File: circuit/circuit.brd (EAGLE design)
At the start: 100 x 80 mm, 56 parts, among them IC1 74HC86N, IC2 74HC86N, IC3 74HC30N, IC4 74HC86N

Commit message: updated circuit (layout needs to be done next)
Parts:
- removed CM4, CM5, CM6: 100nF, rcl:C025-025X050
- removed H1, H2, H3, H4: MOUNT-HOLE3.2, holes:3,2
- removed IC2, IC4: 74HC86N, 74xx-eu:DIL14
- removed IC3: 74HC30N, 74xx-eu:DIL14
- removed JP1: IN, pinhead:1X08
- removed JT: (no value), pinhead:1X04
- removed SJ1, SJ2, SJ3, SJ4, SJ5, SJ6, SJ7, SJ8: (no value), jumper:SJ
- added CS4: 100nF, rcl:C025-025X050
- added LD1, LD2: green, robo_ag:LED_3MM
- added LD3, LD4: yellow, robo_ag:LED_3MM
- added RLD1, RLD2, RLD3, RLD4: 2k, rcl:0207/10
- added RN1, RN2, RN3, RN4: 120, resistor-sil:SIL8
- added RP1: 300, rcl:0207/10
- added X1: PSS 254/8G, con-molex:22-23-2081
- IC1: value 74HC86N -> 74HC04N
- moved SV1 232.4 mm to (-22.2, -292.1)
- moved SV2 228.0 mm to (-22.2, -304.2)
- moved IC1 220.7 mm to (-21.6, -315.0)
- renumbered RP to RP2
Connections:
- removed net BUS_ERROR: IC3.8
- removed net DISP_COL_SCK: JP1.6
- removed net DISP_COL_SER: JP1.4
- removed net PROG_MOSI: ICM.17, RP2.2
- removed net PROG_SCK: ICM.19, JP.3
- removed net RETURN_LED_LAOD: IC2.5
- removed net TWI_SCL: ICM.28, JT.1, JT.4
- removed net TWI_SDA: ICM.27, JT.2, JT.3
- removed net VCC: IC3.14
- new net !BUS_RGB: IC1.1, IC1.3, ICM.3
- new net !RETURN_RGB: IC1.8, ICM.2
- new net N$32: IC1.10, RLD2.2
- new net N$33: JP.3, RP1.2
- new net N$34: LD2.K, RLD2.1
- new net N$35: ICM.27
- new net N$36: ICM.28
- new net N$37: IC1.6, RLD3.2
- new net N$38: LD3.K, RLD3.1
- new net N$41: IC1.12, RLD4.1
- new net N$42: LD4.A, RLD4.2
- new net PROG_MOSI_AND_DISP_COL_SER: ICM.17, RN3.3, RP2.2
- new net PROG_SCK_AND_DISP_COL_SCK: ICM.19, RN3.7, RP1.1
- net +5V: now also CS4.1, LD2.A, LD3.A, X1.2; no longer CM4.2, CM5.2, CM6.2, IC2.14, IC4.14, JP1.2, SJ8.1
- net BTN2: now also ICM.15; no longer ICM.26
- net BTN3: now also ICM.16; no longer ICM.6
- net BUS_BTN_DATA: now also ICM.4, RN1.3; no longer IC2.1, SV1.8
- net BUS_BTN_LOAD: now also ICM.5, RN2.6; no longer IC1.12, SV1.7
- net BUS_CLK: now also ICM.12, RN2.1; no longer IC1.1, SV1.2
- net BUS_IR_CLK: now also ICM.11, RN1.5; no longer IC1.9, SV1.6
- net BUS_LED_DATA: now also IC1.5, ICM.6, RN1.1; no longer IC2.9, SV1.10
- net BUS_LED_LOAD: now also ICM.13, RN2.4; no longer IC2.4, SV1.9
- net BUS_RGB: now also IC1.2, RN1.7; no longer IC1.4, SV1.4
- net DISP_!ENABLE!: now also ICM.26, RN4.3; no longer JP1.8
- net DISP_RCK: now also ICM.25, RN4.1; no longer JP1.7
- net DISP_ROW_SCK: now also ICM.24, RN3.5; no longer JP1.5
- net DISP_ROW_SER: now also ICM.23, RN3.1; no longer JP1.3
- net GND: now also CS4.2, LD1.K, LD4.K, SV1.10, SV1.6, SV1.8, SV2.10, SV2.6, SV2.8, X1.1; no longer CM4.1, CM5.1, CM6.1, IC2.12, IC2.13, IC2.7, IC3.7, IC4.7, JP1.1, SV1.1, SV1.3, SV1.5, SV2.1, SV2.3, SV2.5
- net N$1: now also RN1.2, SV1.1; no longer IC3.1, SJ1.2
- net N$16: now also RN1.8, SV1.7; no longer IC3.4, SJ4.2
- net N$17: now also RN2.2, SV1.9; no longer IC3.5, SJ5.2
- net N$18: now also RN2.5, SV1.4; no longer IC3.6, SJ6.2
- net N$19: now also RN2.3, SV1.2; no longer IC3.11, SJ7.2
- net N$2: now also RN1.4, SV1.3; no longer IC3.2, SJ2.2
- net N$20: now also RN3.2, X1.3; no longer IC3.12, SJ8.2
- net N$21: now also RN3.4, X1.4; no longer IC1.3, SJ1.1
- net N$22: now also RN3.6, X1.5; no longer IC1.6, SJ2.1
- net N$23: now also RN3.8, X1.6; no longer IC1.8, SJ3.1
- net N$24: now also RN4.2, X1.7; no longer IC1.11, SJ4.1
- net N$25: now also RN4.4, X1.8; no longer IC2.3, SJ5.1
- net N$26: now also LD1.A, RLD1.2; no longer IC2.6, SJ6.1
- net N$3: now also RN1.6, SV1.5; no longer IC3.3, SJ3.2
- net N$31: now also IC1.4, RLD1.1; no longer IC2.8, SJ7.1
- net RETURN_BTN_DATA: now also IC1.13, SV2.3; no longer IC2.2, SV2.8
- net RETURN_BTN_LOAD: now also SV2.4; no longer IC1.13, SV2.7
- net RETURN_CLK: now also SV2.9; no longer IC1.2, SV2.2
- net RETURN_IR_CLK: now also SV2.5; no longer IC1.10, SV2.6
- net RETURN_LED_DATA: now also SV2.1; no longer IC2.10, SV2.10
- net RETURN_LED_LOAD: now also SV2.2; no longer SV2.9
- net RETURN_RGB: now also IC1.11, IC1.9, SV2.7; no longer IC1.5, SV2.4
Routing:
- net PROG_SCK: track 53.1 -> 0.00 mm
- net PROG_SCK_AND_DISP_COL_SCK: track 0.00 -> 51.8 mm
- net PROG_MOSI_AND_DISP_COL_SER: track 0.00 -> 41.1 mm
- net PROG_MOSI: track 41.1 -> 0.00 mm
- net BTN2: track 68.5 -> 37.7 mm
- net TWI_SCL: track 15.1 -> 0.00 mm
- net TWI_SDA: track 11.8 -> 0.00 mm

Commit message: Updated Layout
Layout work in progress
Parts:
- removed RN1, RN2, RN3, RN4: 120, resistor-sil:SIL8
- added R1, R10, R11, R12, R13, R2, R3, R4, R5, R6, R7, R8, R9: 120, rcl:R0805
- moved LD4 444.7 mm to (5.71, 45.7), turned to 180 degrees
- moved RLD4 440.8 mm to (15.9, 45.1), turned to 180 degrees
- moved LD3 425.7 mm to (5.08, 36.2)
- moved RLD3 422.0 mm to (16.5, 35.6)
- moved LD1 416.9 mm to (5.71, 41.3), turned to 180 degrees
- moved LD2 411.2 mm to (5.71, 31.1)
- moved RLD1 408.7 mm to (16.5, 40.6), turned to 180 degrees
- moved RLD2 404.3 mm to (16.5, 31.8)
- moved CS4 379.4 mm to (33.7, 49.5), turned to 180 degrees
- moved IC1 358.0 mm to (33.7, 38.7), turned to 270 degrees
- moved SV2 318.6 mm to (43.2, 7.62), turned to 180 degrees
- moved SV1 302.9 mm to (21.6, 7.62), turned to 180 degrees
- moved RP1 301.5 mm to (81.6, 33.7)
- moved X1 278.4 mm to (73.0, 7.30)
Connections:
- removed net N$35: ICM.27
- removed net N$36: ICM.28
- net BTN1: now also ICM.27; no longer ICM.14
- net BTN2: now also ICM.28; no longer ICM.15
- net BUS_BTN_DATA: now also R8.1; no longer RN1.3
- net BUS_BTN_LOAD: now also R13.2; no longer RN2.6
- net BUS_CLK: now also R11.1; no longer RN2.1
- net BUS_IR_CLK: now also R9.1; no longer RN1.5
- net BUS_LED_DATA: now also R7.1; no longer RN1.1
- net BUS_LED_LOAD: now also R12.2; no longer RN2.4
- net BUS_RGB: now also R10.1; no longer RN1.7
- net DISP_!ENABLE!: now also R6.1; no longer RN4.3
- net DISP_RCK: now also R5.1; no longer RN4.1
- net DISP_ROW_SCK: now also R3.1; no longer RN3.5
- net DISP_ROW_SER: now also R1.1; no longer RN3.1
- net N$1: now also R7.2; no longer RN1.2
- net N$16: now also R10.2; no longer RN1.8
- net N$17: now also R11.2; no longer RN2.2
- net N$18: now also R13.1; no longer RN2.5
- net N$19: now also R12.1; no longer RN2.3
- net N$2: now also R8.2; no longer RN1.4
- net N$20: now also R1.2; no longer RN3.2
- net N$21: now also R2.2; no longer RN3.4
- net N$22: now also R3.2; no longer RN3.6
- net N$23: now also R4.2; no longer RN3.8
- net N$24: now also R5.2; no longer RN4.2
- net N$25: now also R6.2; no longer RN4.4
- net N$3: now also R9.2; no longer RN1.6
- net PROG_MOSI_AND_DISP_COL_SER: now also R2.1; no longer RN3.3
- net PROG_SCK_AND_DISP_COL_SCK: now also R4.1; no longer RN3.7
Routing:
- net GND: track 439.4 -> 542.0 mm
- net BTN1: track 79.7 -> 5.08 mm
- net PROG_SCK_AND_DISP_COL_SCK: track 51.8 -> 6.67 mm
- net N$33: track 0.00 -> 36.2 mm
- net BTN2: track 37.7 -> 5.08 mm
- net BTN3: track 27.1 -> 5.08 mm
- net +5V: track 448.4 -> 432.8 mm, vias 6 -> 7
- net N$19: track 0.00 -> 11.3 mm
- net N$18: track 0.00 -> 10.3 mm
- net N$1: track 0.00 -> 7.72 mm
- net N$3: track 0.00 -> 6.67 mm
- net N$2: track 0.00 -> 6.67 mm
- net N$17: track 0.00 -> 6.67 mm
- net N$16: track 0.00 -> 6.67 mm
- net RESET: track 41.8 -> 48.0 mm
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- removed copper zone on layer 1, net GND
- removed copper zone on layer 16, net GND

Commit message: minor changes
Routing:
- net GND: track 542.0 -> 531.0 mm, vias 6 -> 3
- net +5V: track 432.8 -> 427.0 mm, vias 7 -> 4
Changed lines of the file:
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@@
 <wire x1="85.09" y1="64.389" x2="86.995" y2="66.294" width="1.27" layer="16"/>
 <via x="93.345" y="36.195" extent="1-16" drill="0.8" diameter="1.4224"/>
-<wire x1="93.345" y1="36.195" x2="93.98" y2="36.195" width="1.27" layer="16"/>
+<wire x1="93.345" y1="36.195" x2="93.98" y2="36.195" width="0" layer="19" extent="1-16"/>
 <wire x1="97.79" y1="27.305" x2="96.52" y2="28.575" width="1.27" layer="1"/>
-<wire x1="93.345" y1="28.575" x2="93.345" y2="34.6075" width="1.27" layer="1"/>
-<wire x1="93.345" y1="34.6075" x2="93.345" y2="36.195" width="1.27" layer="1"/>
+<wire x1="93.345" y1="28.575" x2="93.345" y2="36.195" width="1.27" layer="1"/>
+<wire x1="93.345" y1="34.6075" x2="93.345" y2="36.195" width="0" layer="19" extent="1-16"/>
 <wire x1="96.52" y1="28.575" x2="93.345" y2="28.575" width="1.27" layer="1"/>
-<wire x1="93.345" y1="36.195" x2="93.345" y2="37.7825" width="1.27" layer="1"/>
+<wire x1="93.345" y1="36.195" x2="93.345" y2="37.7825" width="0" layer="19" extent="1-16"/>
 <via x="93.345" y="50.165" extent="1-16" drill="0.8" diameter="1.4224"/>
-<wire x1="93.345" y1="37.7825" x2="93.345" y2="50.165" width="1.27" layer="1"/>
-<wire x1="93.345" y1="50.165" x2="93.345" y2="51.7525" width="1.27" layer="16"/>
-<via x="93.345" y="34.6075" extent="1-16" drill="0.8" diameter="1.4224"/>
-<via x="93.345" y="37.7825" extent="1-16" drill="0.8" diameter="1.4224"/>
-<wire x1="93.345" y1="51.7525" x2="93.345" y2="58.42" width="1.27" layer="16"/>
-<wire x1="93.345" y1="37.7825" x2="93.345" y2="34.6075" width="1.27" layer="16"/>
-<via x="93.345" y="51.7525" extent="1-16" drill="0.8" diameter="1.4224"/>
-<wire x1="93.345" y1="34.29" x2="93.345" y2="34.6075" width="1.27" layer="16"/>
-<wire x1="93.345" y1="51.7525" x2="93.345" y2="50.165" width="1.27" layer="1"/>
+<wire x1="93.345" y1="36.195" x2="93.345" y2="50.165" width="1.27" layer="1"/>
+<wire x1="93.345" y1="50.165" x2="93.345" y2="51.7525" width="0" layer="19" extent="1-16"/>
+<wire x1="93.345" y1="34.6075" x2="93.345" y2="34.6075" width="0" layer="19" extent="1-16"/>
+<wire x1="93.345" y1="37.7825" x2="93.345" y2="37.7825" width="0" layer="19" extent="1-16"/>
+<wire x1="93.345" y1="50.165" x2="93.345" y2="58.42" width="1.27" layer="16"/>
+<wire x1="93.345" y1="37.7825" x2="93.345" y2="34.29" width="0" layer="19" extent="1-16"/>
+<wire x1="93.345" y1="51.7525" x2="93.345" y2="51.7525" width="0" layer="19" extent="1-16"/>
+<wire x1="93.345" y1="34.29" x2="93.345" y2="34.6075" width="0" layer="19" extent="1-16"/>
+<wire x1="93.345" y1="51.7525" x2="93.345" y2="50.165" width="0" layer="19" extent="1-16"/>
 <wire x1="58.42" y1="43.815" x2="60.96" y2="41.275" width="0.4064" layer="16"/>
 <wire x1="60.96" y1="41.275" x2="62.23" y2="41.275" width="0.4064" layer="16"/>
@@
 <wire x1="73.66" y1="66.675" x2="73.66" y2="66.04" width="0.3048" layer="1"/>
 <wire x1="1.905" y1="11.43" x2="1.905" y2="64.135" width="1.27" layer="16"/>
-<wire x1="91.44" y1="25.7175" x2="91.44" y2="27.305" width="1.27" layer="1"/>
-<wire x1="91.44" y1="27.305" x2="92.71" y2="28.575" width="1.27" layer="16"/>
+<wire x1="91.44" y1="25.7175" x2="91.44" y2="27.305" width="0" layer="19" extent="1-16"/>
+<wire x1="91.44" y1="27.305" x2="92.71" y2="28.575" width="0" layer="19" extent="1-16"/>
 <wire x1="92.71" y1="28.575" x2="96.52" y2="28.575" width="1.27" layer="16"/>
-<via x="91.44" y="27.305" extent="1-16" drill="0.8" diameter="1.4224"/>
+<wire x1="91.44" y1="27.305" x2="91.44" y2="27.305" width="0" layer="19" extent="1-16"/>
 <wire x1="93.345" y1="63.5" x2="93.345" y2="68.58" width="1.27" layer="16"/>
 <wire x1="93.345" y1="68.58" x2="86.995" y2="68.58" width="1.27" layer="16"/>
@@
 <wire x1="86.995" y1="68.326" x2="86.995" y2="68.58" width="1.27" layer="16"/>
 <wire x1="85.725" y1="74.93" x2="85.725" y2="68.58" width="1.27" layer="16"/>
-<via x="91.44" y="25.7175" extent="1-16" drill="0.8" diameter="1.4224"/>
-<wire x1="91.44" y1="27.305" x2="91.44" y2="25.7175" width="1.27" layer="16"/>
+<wire x1="91.44" y1="25.7175" x2="91.44" y2="25.7175" width="0" layer="19" extent="1-16"/>
+<wire x1="91.44" y1="27.305" x2="91.44" y2="25.7175" width="0" layer="19" extent="1-16"/>
 <wire x1="97.79" y1="49.53" x2="96.52" y2="48.26" width="1.27" layer="16"/>
 <wire x1="96.52" y1="48.26" x2="93.345" y2="48.26" width="1.27" layer="16"/>
-<wire x1="91.44" y1="47.625" x2="91.44" y2="46.0375" width="1.27" layer="1"/>
-<via x="91.44" y="47.625" extent="1-16" drill="0.8" diameter="1.4224"/>
+<wire x1="91.44" y1="47.625" x2="91.44" y2="46.0375" width="0" layer="19" extent="1-16"/>
+<wire x1="91.44" y1="47.625" x2="91.44" y2="47.625" width="0" layer="19" extent="1-16"/>
 <wire x1="91.44" y1="46.0375" x2="91.44" y2="39.37" width="1.27" layer="1"/>
 <wire x1="91.44" y1="39.37" x2="91.44" y2="28.8925" width="1.27" layer="1"/>
-<wire x1="91.44" y1="28.8925" x2="91.44" y2="27.305" width="1.27" layer="1"/>
+<wire x1="91.44" y1="28.8925" x2="91.44" y2="27.305" width="0" layer="19" extent="1-16"/>
 <via x="91.44" y="28.8925" extent="1-16" drill="0.8" diameter="1.4224"/>
-<wire x1="91.44" y1="28.8925" x2="91.44" y2="27.305" width="1.27" layer="16"/>
+<wire x1="91.44" y1="28.8925" x2="91.44" y2="27.305" width="0" layer="19" extent="1-16"/>
 <via x="91.44" y="46.0375" extent="1-16" drill="0.8" diameter="1.4224"/>
-<wire x1="91.44" y1="46.355" x2="91.44" y2="47.625" width="1.27" layer="16"/>
+<wire x1="91.44" y1="46.355" x2="91.44" y2="47.625" width="0" layer="19" extent="1-16"/>
 <wire x1="93.345" y1="48.26" x2="91.44" y2="46.355" width="1.27" layer="16"/>
 <wire x1="91.44" y1="46.355" x2="91.44" y2="46.0375" width="1.27" layer="16"/>

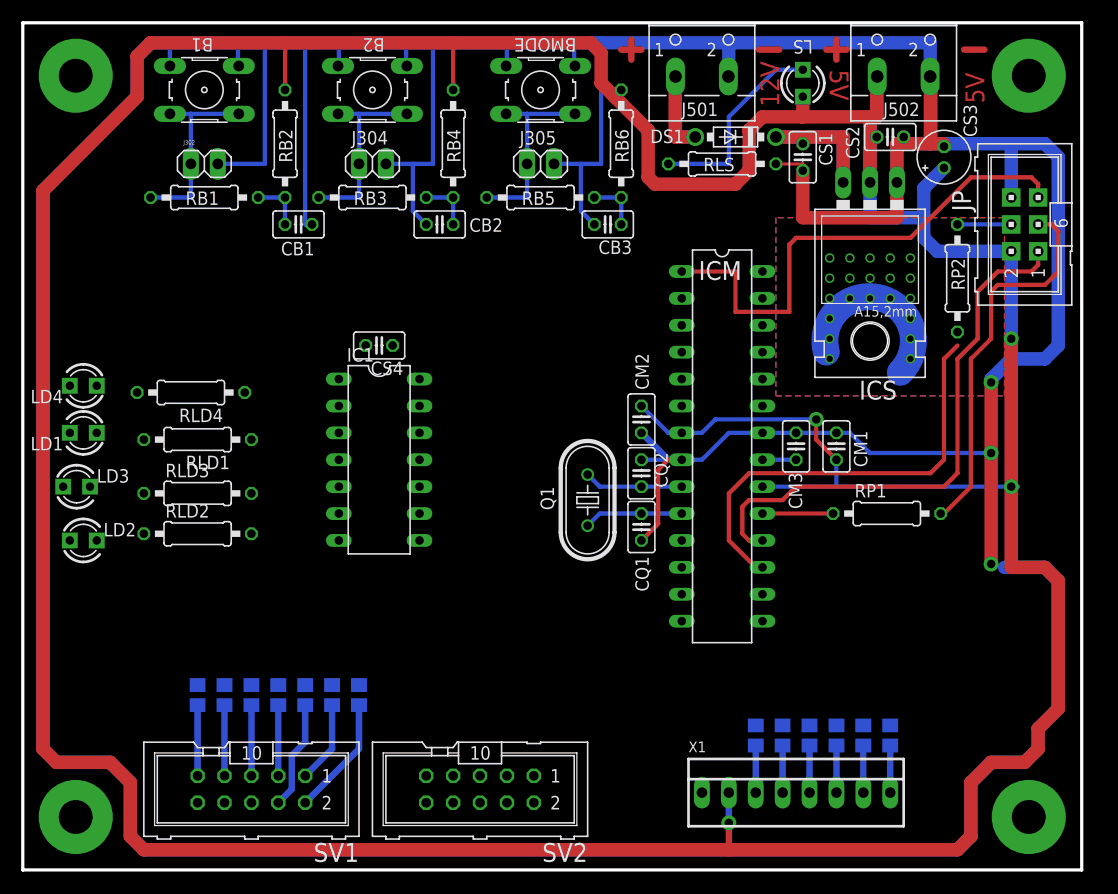
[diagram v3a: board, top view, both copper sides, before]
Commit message: Layout nearly completed
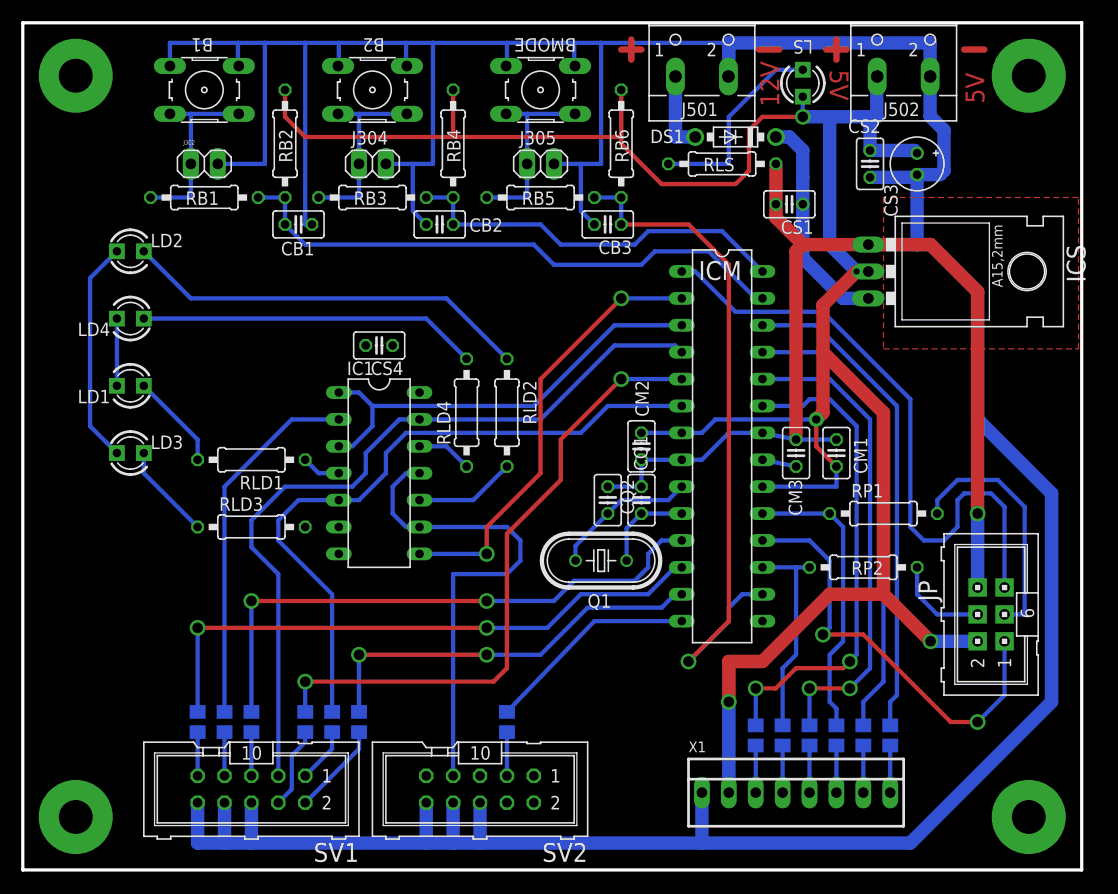
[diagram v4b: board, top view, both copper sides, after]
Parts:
- moved JP 37.0 mm to (91.4, 24.1)
- moved RLD2 31.4 mm to (45.7, 43.2), turned to 270 degrees
- moved RP2 28.7 mm to (79.4, 28.6), turned to 180 degrees
- moved LD2 27.7 mm to (10.2, 58.4)
- moved RLD4 26.1 mm to (41.9, 43.2), turned to 90 degrees
- moved R8 21.7 mm to (45.7, 14.0)
- moved LD4 7.75 mm to (10.2, 52.1)
- moved LD1 6.29 mm to (10.2, 45.7)
- moved RLD3 5.99 mm to (21.6, 32.4)
- moved LD3 5.99 mm to (10.2, 39.4)
- moved ICS 5.88 mm to (83.7, 56.5), turned to 270 degrees
- moved Q1 5.85 mm to (54.6, 29.2), turned to 180 degrees
- moved RLD1 5.43 mm to (21.6, 38.7)
- moved CS1 4.62 mm to (72.4, 62.9), turned to 180 degrees
- moved CQ2 4.07 mm to (55.2, 34.9)
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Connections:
- net BUS_BTN_DATA: now also IC1.13, SV1.3; no longer R8.1
- net N$2: now also SV2.3; no longer SV1.3
- net RETURN_BTN_DATA: now also ICM.14, R8.1; no longer IC1.13, SV2.3
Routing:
- net +5V: track 427.0 -> 239.8 mm, vias 4 -> 5
- net BUS_BTN_DATA: track 0.00 -> 74.0 mm
- net GND: track 531.0 -> 465.7 mm, vias 3 -> 1
- net BUS_LED_DATA: track 0.00 -> 63.9 mm
- net BTN3: track 5.08 -> 66.2 mm, vias 0 -> 1
- net BUS_BTN_LOAD: track 0.00 -> 59.9 mm, vias 0 -> 2
- net BUS_CLK: track 0.00 -> 56.0 mm, vias 0 -> 2
- net BUS_IR_CLK: track 0.00 -> 54.2 mm, vias 0 -> 2
- net BTN1: track 5.08 -> 54.1 mm
- net RETURN_RGB: track 0.00 -> 46.6 mm
- net DISP_!ENABLE!: track 0.00 -> 46.3 mm
- net DISP_ROW_SER: track 0.00 -> 46.1 mm, vias 0 -> 2
- net DISP_ROW_SCK: track 0.00 -> 45.2 mm, vias 0 -> 2
- net DISP_RCK: track 0.00 -> 44.1 mm
- net !BUS_RGB: track 0.00 -> 41.9 mm
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- removed copper zone on layer 16, net ICS_TAB

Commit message: Layout finished
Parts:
- moved LD1 8.13 mm to (15.2, 52.1), turned to 0 degrees
- moved LD4 8.13 mm to (15.2, 45.7), turned to 0 degrees
- moved RLD1 7.24 mm to (26.0, 44.5), turned to 90 degrees
- moved LD2 5.08 mm to (15.2, 58.4)
- moved LD3 5.08 mm to (15.2, 39.4)
- moved R13 5.08 mm to (31.8, 14.0)
- moved R12 2.54 mm to (29.2, 14.0)
- moved R7 2.54 mm to (26.7, 14.0)
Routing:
- net +5V: track 239.8 -> 293.9 mm, vias 5 -> 6
- net GND: track 465.7 -> 501.2 mm, vias 1 -> 4
- net N$18: track 7.72 -> 16.2 mm
- net RETURN_RGB: track 46.6 -> 39.1 mm
- net N$26: track 9.09 -> 16.3 mm
- net BUS_BTN_LOAD: track 59.9 -> 53.9 mm
- net N$34: track 38.5 -> 33.4 mm
- net N$42: track 32.1 -> 35.9 mm
- net N$37: track 0.00 -> 3.17 mm
- net N$38: track 9.09 -> 6.98 mm
- net BUS_LED_LOAD: track 38.2 -> 40.0 mm
- net !RETURN_RGB: track 41.5 -> 40.0 mm
- net BUS_LED_DATA: track 63.9 -> 62.8 mm
- net N$19: track 8.77 -> 7.72 mm
- net N$1: track 5.18 -> 4.13 mm
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- added copper zone on layer 1, net N$35
- added copper zone on layer 16, net N$35
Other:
- board text added: "Btn"
- board text added: "Bus"
- board text added: "Display"
- board text added: "LED"
- board text added: "Light Bus"
- board text added: "RGB"
- board text added: "Retrn"
- board text added: "Return"
- board text added: "RoboSAX 2018"
